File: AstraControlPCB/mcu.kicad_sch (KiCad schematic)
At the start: 9 parts, among them U1 ESP32-S3-WROOM-1U-N8

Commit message: Updated Pi filter
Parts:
- removed C1: 47u, LiveAstra:C_0805_2012Metric_Pad1.18x1.45mm_HandSolder, symbol LiveAstra:C_47u_X5R_0805
- added C1: 22u, LiveAstra:C_0603_1608Metric, symbol LiveAstra:C_22uF_X5R_0603
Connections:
- net 3V3: now also C1.2
- net GND: now also C1.1
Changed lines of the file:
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@@
+	)
+	(symbol
+		(lib_id "LiveAstra:C_22uF_X5R_0603")
+		(at 33.02 53.34 90)
+		(unit 1)
+		(exclude_from_sim no)
+		(in_bom yes)
+		(on_board yes)
+		(dnp no)
+		(fields_autoplaced yes)
+		(property "Reference" "C1"
+			(at 36.83 50.7999 90)
+			(effects
+				(font
+					(size 1.27 1.27)
+				)
+				(justify right)
+			)
+		)
+		(property "Value" "22u"
+			(at 36.83 53.34 90)
+			(effects
+				(font
+					(size 1.27 1.27)
+					(bold yes)
+				)
+				(justify right)
+			)
+		)
+		(property "Footprint" "LiveAstra:C_0603_1608Metric"
+			(at 41.91 53.34 0)
+			(effects
+				(font
+					(size 1.27 1.27)
+				)
+				(hide yes)
+			)
+		)
+		(property "Datasheet" "https://lcsc.com/product-detail/Multilayer-Ceramic-Capacitors-MLCC-SMD-SMT_SAMSUNG_CL10A226MQ8NRNC_22uF-226-20-6-3V_C59461.html"
+			(at 45.72 53.34 0)
+			(effects
+				(font
+					(size 1.27 1.27)
+				)
+				(hide yes)
+			)
+		)
+		(property "Description" "6.3V 22uF X5R ±20% 0603 Multilayer Ceramic Capacitors MLCC - SMD/SMT ROHS"
+			(at 38.1 53.34 0)
+			(effects
+				(font
+					(size 1.27 1.27)
+				)
+				(hide yes)
+			)
+		)
+		(property "LCSC Part" "C59461"
+			(at 49.53 53.34 0)
+			(effects
+				(font
+					(size 1.27 1.27)
+				)
+				(hide yes)
+			)
+		)
+		(property "Extra Values" "6.3V X5R 20% 0603"
+			(at 36.83 55.8799 90)
+			(effects
+				(font
+					(size 0.762 0.762)
+					(bold yes)
+				)
+				(justify right)
+			)
+		)
+		(property "MPN" "CL10A226MQ8NRNC"
+			(at 53.34 53.34 0)
+			(effects
+				(font
+					(size 1.27 1.27)
+				)
+				(hide yes)
+			)
+		)
+		(property "MFN" "Samsung Electro-Mechanics"
+			(at 57.15 53.34 0)
+			(effects
+				(font
+					(size 1.27 1.27)
+				)
+				(hide yes)
+			)
+		)
+		(pin "2"
+		)
+		(pin "1"
+		)
+		(instances
+			(project ""
+				(path "/9a751838-dce8-4d69-8a02-736625ac74e7/0db21d8e-3390-4d67-877f-0e5d98e37848/3087dd4a-2a8a-4df4-b1d8-8d4a2b3256a2"
+					(reference "C1")
+					(unit 1)
+				)
+			)
+		)
 	)
 	(symbol
@@
 					(unit 1)
 				)
-			)
-		)
-	)
-	(symbol
-		(lib_id "LiveAstra:C_47u_X5R_0805")
-		(at 33.02 53.34 90)
-		(unit 1)
-		(exclude_from_sim no)
-		(in_bom yes)
-		(on_board yes)
-		(dnp no)
-		(fields_autoplaced yes)
-		(property "Reference" "C1"
-			(at 36.83 50.7999 90)
-			(effects
-				(font
-					(size 1.27 1.27)
-				)
-				(justify right)
-			)
-		)
-		(property "Value" "47u"
-			(at 36.83 53.34 90)
-			(effects
-				(font
-					(size 1.27 1.27)
-					(bold yes)
-				)
-				(justify right)
-			)
-		)
-		(property "Footprint" "LiveAstra:C_0805_2012Metric_Pad1.18x1.45mm_HandSolder"
-			(at 41.91 53.34 0)
-			(effects
-				(font
-					(size 1.27 1.27)
-				)
-				(hide yes)
-			)
-		)
-		(property "Datasheet" "https://lcsc.com/product-detail/Multilayer-Ceramic-Capacitors-MLCC-SMD-SMT_SAMSUNG_CL21A476MQYNNNE_47uF-476-20-6-3V_C16780.html"
-			(at 45.72 53.34 0)
-			(effects
-				(font
-					(size 1.27 1.27)
-				)
-				(hide yes)
-			)
-		)
-		(property "Description" "6.3V 47uF X5R ±20% 0805 Multilayer Ceramic Capacitors MLCC - SMD/SMT ROHS"
-			(at 38.1 53.34 0)
-			(effects
-				(font
-					(size 1.27 1.27)
-				)
-				(hide yes)
-			)
-		)
-		(property "LCSC Part" "C16780"
-			(at 49.53 53.34 0)
-			(effects
-				(font
-					(size 1.27 1.27)
-				)
-				(hide yes)
-			)
-		)
-		(property "Extra Values" "6.3V X5R 20% 0805"
-			(at 36.83 55.8799 90)
-			(effects
-				(font
-					(size 0.762 0.762)
-					(bold yes)
-				)
-				(justify right)
-			)
-		)
-		(property "MFN" "Samsung Electro-Mechanics"
-			(at 53.34 53.34 0)
-			(effects
-				(font
-					(size 1.27 1.27)
-				)
-				(hide yes)
-			)
-		)
-		(property "MPN" "CL21A476MQYNNNE"
-			(at 53.34 53.34 0)
-			(effects
-				(font
-					(size 1.27 1.27)
-				)
-				(hide yes)
-			)
-		)
-		(pin "1"
-		)
-		(pin "2"
-		)
-		(instances
-			(project ""
-				(path "/9a751838-dce8-4d69-8a02-736625ac74e7/0db21d8e-3390-4d67-877f-0e5d98e37848/3087dd4a-2a8a-4df4-b1d8-8d4a2b3256a2"
-					(reference "C1")
-					(unit 1)
-				)

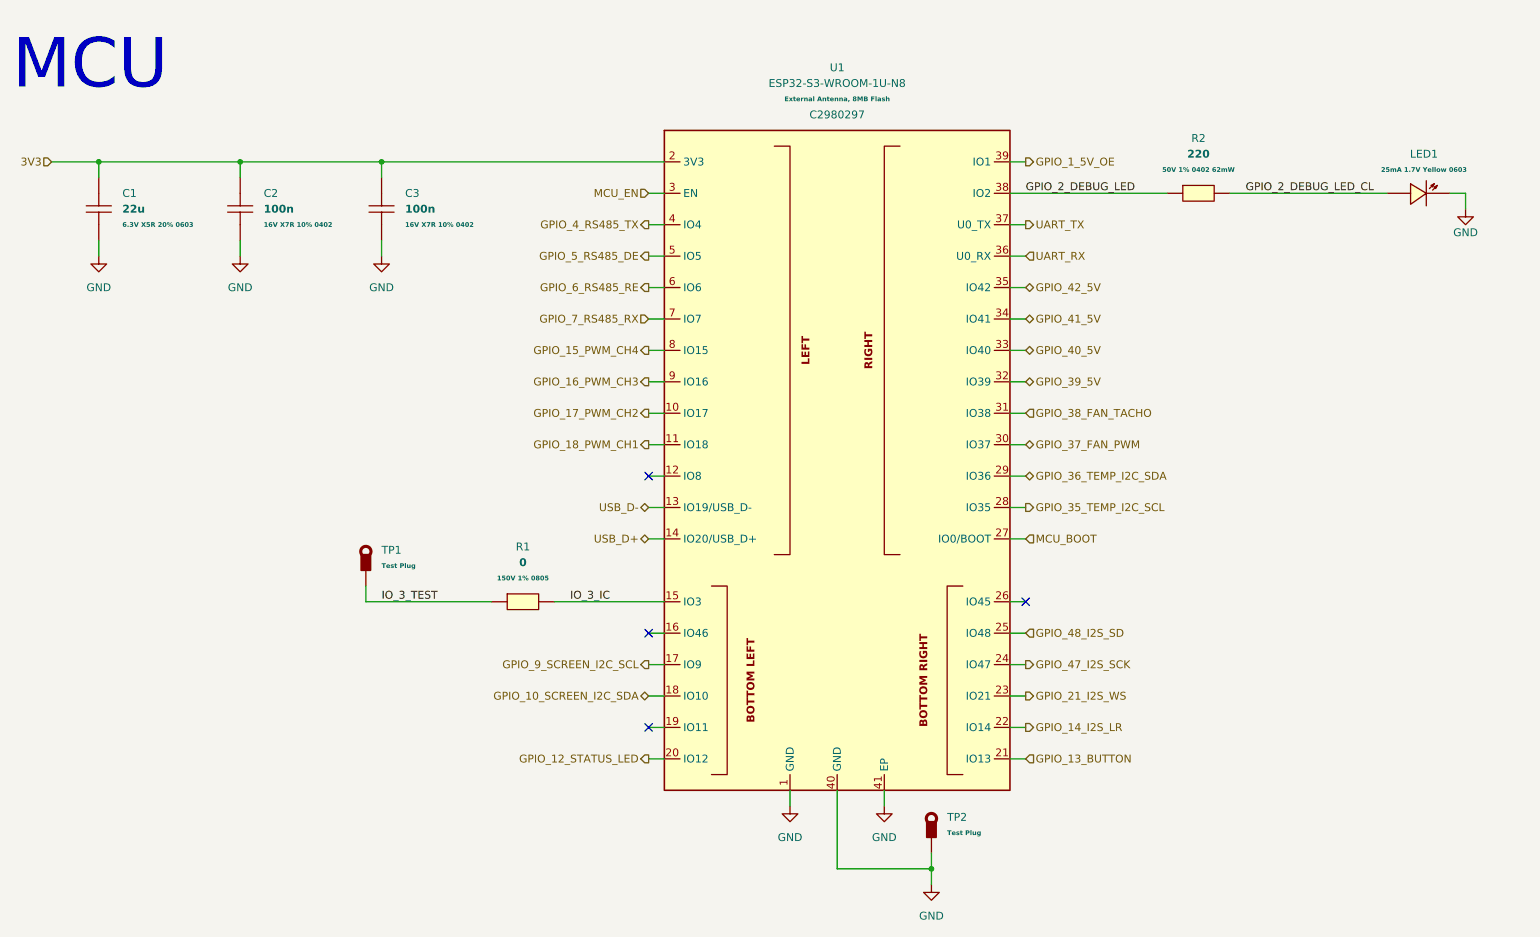
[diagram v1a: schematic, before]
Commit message: Update to new rs485 chip, use 2 bit 5v gpio
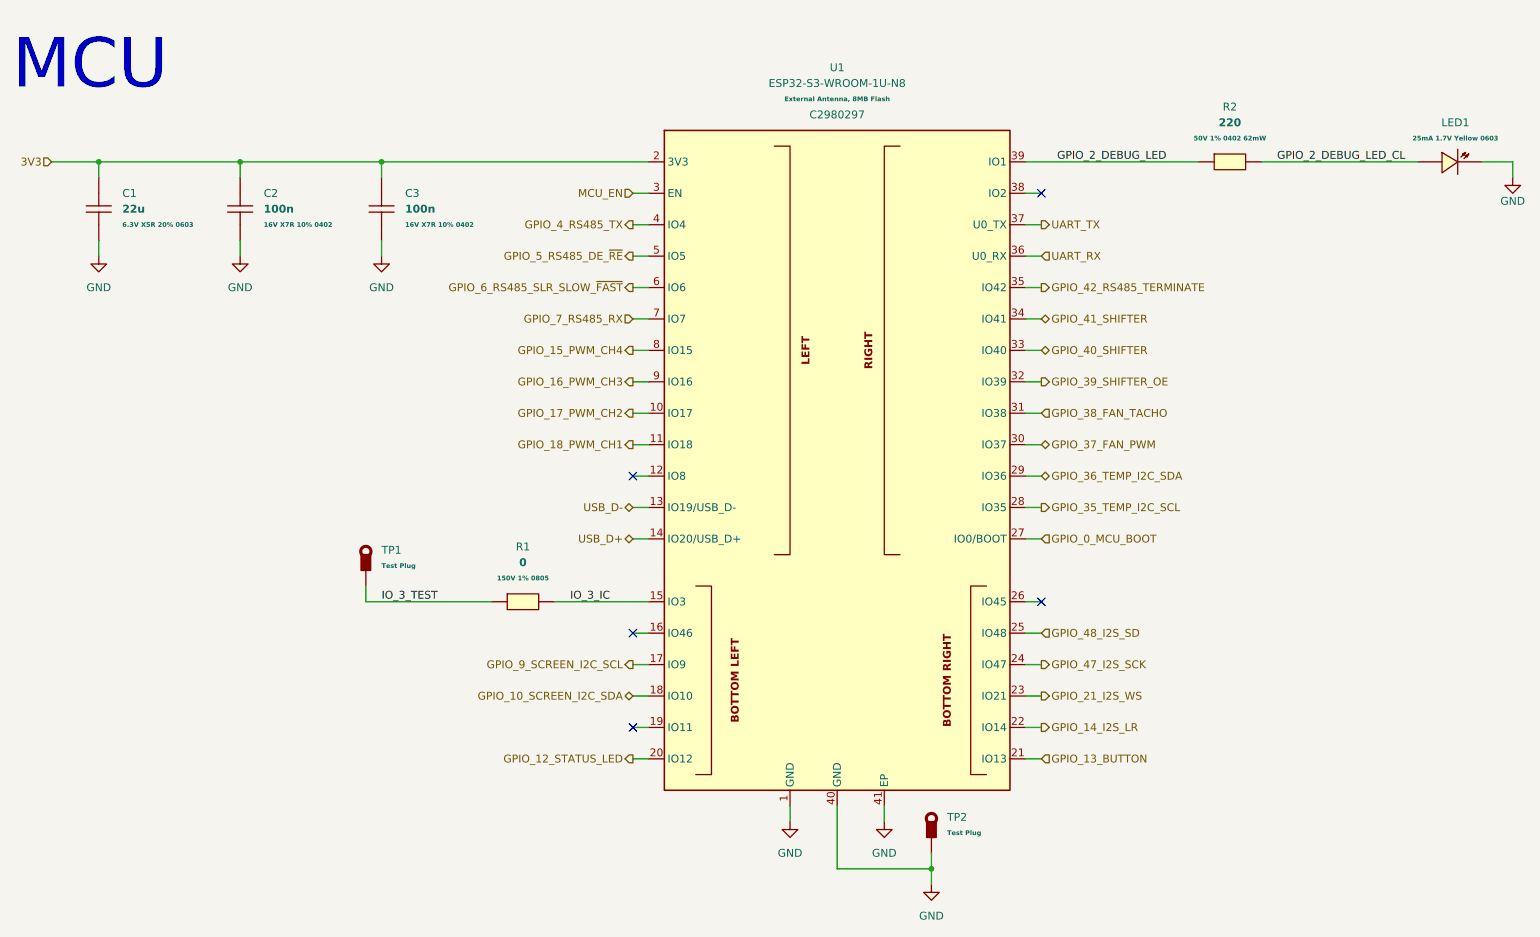
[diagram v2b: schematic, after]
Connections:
- net GPIO_1_5V_OE is gone; now on net GPIO_2_DEBUG_LED: U1.39 (IO1)
- net GPIO_2_DEBUG_LED: no longer U1.38 (IO2)
- net GPIO_39_5V renamed GPIO_39_SHIFTER_OE
- net GPIO_40_5V renamed GPIO_40_SHIFTER
- net GPIO_41_5V renamed GPIO_41_SHIFTER
- net GPIO_42_5V renamed GPIO_42_RS485_TERMINATE
- net GPIO_5_RS485_DE renamed GPIO_5_RS485_DE_~{RE}
- net GPIO_6_RS485_RE renamed GPIO_6_RS485_SLR_SLOW_~{FAST}
- net MCU_BOOT renamed GPIO_0_MCU_BOOT
- no-connect marks 4 -> 5
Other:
- moved on the sheet: LED1, R2, U1

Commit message: Cleanup
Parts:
- added INF9: ~, symbol LiveAstra:Information_Box
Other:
- note added: "Strapping Pins: GPIO 0 pull-up, GPIO 3 Floating, GPIO 45 pull down, GPIO 46 pull down."
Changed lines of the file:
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@@
+		)
+	)
+	(text "Strapping Pins: \nGPIO 0 pull-up, GPIO 3 Floating,\nGPIO 45 pull down, GPIO 46 pull down.\n"
+		(exclude_from_sim no)
+		(at 22.86 104.14 0)
+		(effects
+			(font
+				(face "ING Me")
+				(size 1.397 1.397)
+			)
+			(justify left)
 		)
 	)
@@
 					(unit 1)
 				)
+			)
+		)
+	)
+	(symbol
+		(lib_id "LiveAstra:Information_Box")
+		(at 45.72 101.6 0)
+		(unit 1)
+		(exclude_from_sim yes)
+		(in_bom no)
+		(on_board no)
+		(dnp no)
+		(fields_autoplaced yes)
+		(property "Reference" "INF9"
+			(at 45.72 90.17 0)
+			(effects
+				(font
+					(size 1.27 1.27)
+				)
+			)
+		)
+		(property "Value" "~"
+			(at 45.72 92.71 0)
+			(effects
+				(font
+					(size 1.27 1.27)
+				)
+			)
+		)
+		(property "Footprint" ""
+			(at 30.48 97.79 0)
+			(effects
+				(font
+					(size 1.27 1.27)
+				)
+				(hide yes)
+			)
+		)
+		(property "Datasheet" ""
+			(at 30.48 97.79 0)
+			(effects
+				(font
+					(size 1.27 1.27)
+				)
+				(hide yes)
+			)
+		)
+		(property "Description" ""
+			(at 30.48 97.79 0)
+			(effects
+				(font
+					(size 1.27 1.27)
+				)
+				(hide yes)
+			)
+		)
+		(instances
+			(project "AstraControl"
+				(path "/9a751838-dce8-4d69-8a02-736625ac74e7/0db21d8e-3390-4d67-877f-0e5d98e37848/3087dd4a-2a8a-4df4-b1d8-8d4a2b3256a2"
+					(reference "INF9")
+					(unit 1)
+				)

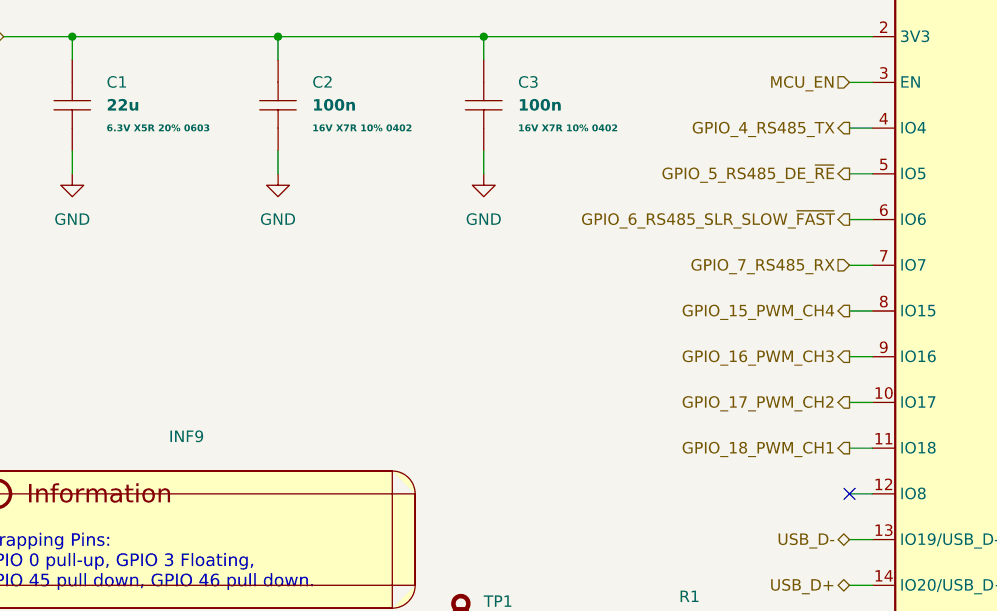
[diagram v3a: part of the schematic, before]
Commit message: New inductor that is in stock, updated rs485 ic layout to put caps closer
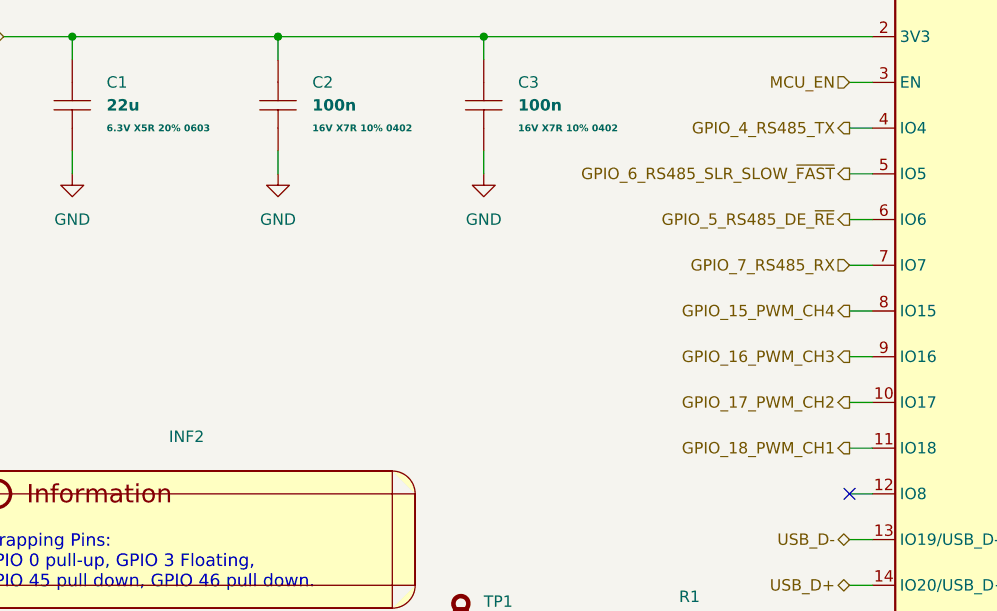
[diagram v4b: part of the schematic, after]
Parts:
- renumbered INF9 to INF2
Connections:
- net GPIO_5_RS485_DE_~{RE}: now also U1.6 (IO6); no longer U1.5 (IO5)
- net GPIO_6_RS485_SLR_SLOW_~{FAST}: now also U1.5 (IO5); no longer U1.6 (IO6)
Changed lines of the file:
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@@
+	(wire
+		(pts
+			(xy 119.38 60.96) (xy 121.92 60.96)
+		)
+		(stroke
+			(width 0)
+			(type default)
+		)
+	)
 	(wire
 		(pts
@@
 	(wire
 		(pts
+			(xy 261.62 45.72) (xy 256.54 45.72)
+		)
+		(stroke
+			(width 0)
+			(type default)
+		)
+	)
+	(wire
+		(pts
+			(xy 185.42 116.84) (xy 182.88 116.84)
+		)
+		(stroke
+			(width 0)
+			(type default)
+		)
+	)
+	(wire
+		(pts
+			(xy 106.68 116.84) (xy 121.92 116.84)
+		)
+		(stroke
+			(width 0)
+			(type default)
+		)
+	)
+	(wire
+		(pts
+			(xy 76.2 116.84) (xy 96.52 116.84)
+		)
+		(stroke
+			(width 0)
+			(type default)
+		)
+	)
+	(wire
+		(pts
+			(xy 185.42 132.08) (xy 182.88 132.08)
+		)
+		(stroke
+			(width 0)
+			(type default)
+		)
+	)
+	(wire
+		(pts
+			(xy 185.42 91.44) (xy 182.88 91.44)
+		)
+		(stroke
+			(width 0)
+			(type default)
+		)
+	)
+	(wire
+		(pts
+			(xy 185.42 121.92) (xy 182.88 121.92)
+		)
+		(stroke
+			(width 0)
+			(type default)
+		)
+	)
+	(wire
+		(pts
+			(xy 185.42 55.88) (xy 182.88 55.88)
+		)
+		(stroke
+			(width 0)
+			(type default)
+		)
+	)
+	(wire
+		(pts
+			(xy 185.42 101.6) (xy 182.88 101.6)
+		)
+		(stroke
+			(width 0)
+			(type default)
+		)
+	)
+	(wire
+		(pts
+			(xy 55.88 60.96) (xy 55.88 58.42)
+		)
+		(stroke
+			(width 0)
+			(type default)
+		)
+	)
+	(wire
+		(pts
+			(xy 119.38 132.08) (xy 121.92 132.08)
+		)
+		(stroke
+			(width 0)
+			(type default)
+		)
+	)
+	(wire
+		(pts
+			(xy 119.38 137.16) (xy 121.92 137.16)
+		)
+		(stroke
+			(width 0)
+			(type default)
+		)
+	)
+	(wire
+		(pts
+			(xy 182.88 50.8) (xy 185.42 50.8)
+		)
+		(stroke
+			(width 0)
+			(type default)
+		)
+	)
+	(wire
+		(pts
 			(xy 119.38 66.04) (xy 121.92 66.04)
-		)
-		(stroke
-			(width 0)
-			(type default)
-		)
-	)
-	(wire
-		(pts
-			(xy 261.62 45.72) (xy 256.54 45.72)
-		)
-		(stroke
-			(width 0)
-			(type default)
-		)
-	)
-	(wire
-		(pts
-			(xy 185.42 116.84) (xy 182.88 116.84)
-		)
-		(stroke
-			(width 0)
-			(type default)
-		)
-	)
-	(wire
-		(pts
-			(xy 106.68 116.84) (xy 121.92 116.84)
-		)
-		(stroke
-			(width 0)
-			(type default)
-		)
-	)
-	(wire
-		(pts
-			(xy 76.2 116.84) (xy 96.52 116.84)
-		)
-		(stroke
-			(width 0)
-			(type default)
-		)
-	)
-	(wire
-		(pts
-			(xy 185.42 132.08) (xy 182.88 132.08)
-		)
-		(stroke
-			(width 0)
-			(type default)
-		)
-	)
-	(wire
-		(pts
-			(xy 185.42 91.44) (xy 182.88 91.44)
-		)
-		(stroke
-			(width 0)
-			(type default)
-		)
-	)
-	(wire
-		(pts
-			(xy 185.42 121.92) (xy 182.88 121.92)
-		)
-		(stroke
-			(width 0)
-			(type default)
-		)
-	)
-	(wire
-		(pts
-			(xy 185.42 55.88) (xy 182.88 55.88)
-		)
-		(stroke
-			(width 0)
-			(type default)
-		)
-	)
-	(wire
-		(pts
-			(xy 185.42 101.6) (xy 182.88 101.6)
-		)
-		(stroke
-			(width 0)
-			(type default)
-		)
-	)
-	(wire
-		(pts
-			(xy 119.38 60.96) (xy 121.92 60.96)
-		)
-		(stroke
-			(width 0)
-			(type default)
-		)
-	)
-	(wire
-		(pts
-			(xy 55.88 60.96) (xy 55.88 58.42)
-		)
-		(stroke
-			(width 0)
-			(type default)
-		)
-	)
-	(wire
-		(pts
-			(xy 119.38 132.08) (xy 121.92 132.08)
-		)
-		(stroke
-			(width 0)
-			(type default)
-		)
-	)
-	(wire
-		(pts
-			(xy 119.38 137.16) (xy 121.92 137.16)
-		)
-		(stroke
-			(width 0)
-			(type default)
-		)
-	)
-	(wire
-		(pts
-			(xy 182.88 50.8) (xy 185.42 50.8)
 		)
 		(stroke
@@
 	(hierarchical_label "GPIO_5_RS485_DE_~{RE}"
 		(shape output)
-		(at 119.38 60.96 180)
+		(at 119.38 66.04 180)
 		(fields_autoplaced yes)
 		(effects
@@
 	(hierarchical_label "GPIO_6_RS485_SLR_SLOW_~{FAST}"
 		(shape output)
-		(at 119.38 66.04 180)
+		(at 119.38 60.96 180)
 		(fields_autoplaced yes)
 		(effects
@@
 		(dnp no)
 		(fields_autoplaced yes)
-		(property "Reference" "INF9"
+		(property "Reference" "INF2"
 			(at 45.72 90.17 0)
 			(effects
@@
 			(project "AstraControl"
 				(path "/9a751838-dce8-4d69-8a02-736625ac74e7/0db21d8e-3390-4d67-877f-0e5d98e37848/3087dd4a-2a8a-4df4-b1d8-8d4a2b3256a2"
-					(reference "INF9")
+					(reference "INF2")
 					(unit 1)
 				)

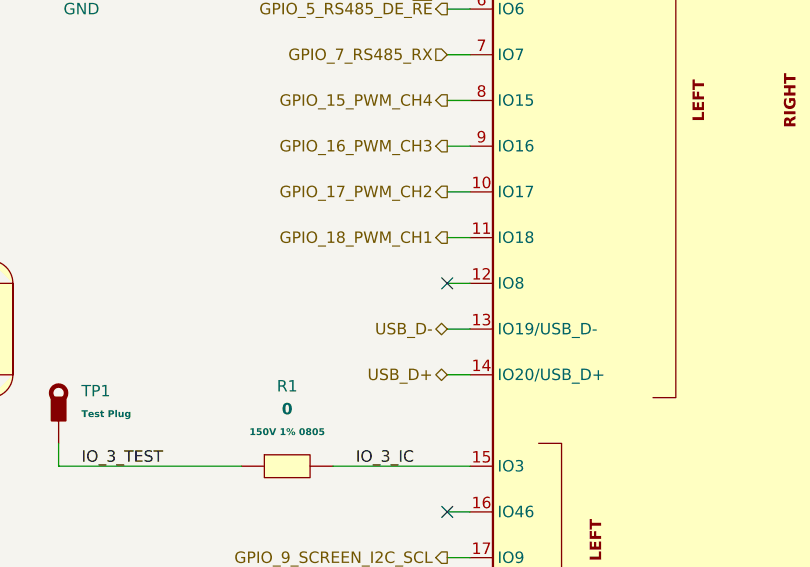
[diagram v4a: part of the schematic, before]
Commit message: Fix silkscreen on copper, add GPIO 8 to connector
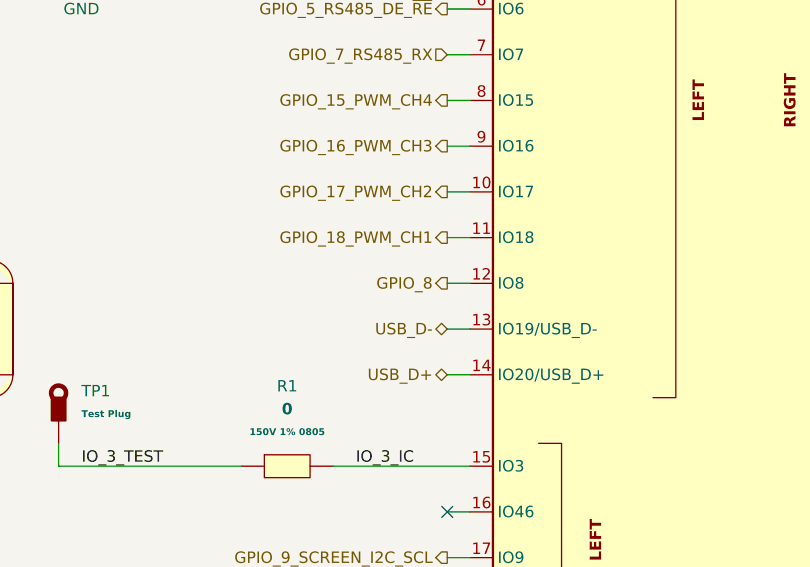
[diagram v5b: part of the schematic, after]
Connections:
- net GPIO_8: now reaches U1.12 (IO8)
- no-connect marks 5 -> 4
